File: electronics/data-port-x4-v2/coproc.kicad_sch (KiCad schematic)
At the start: 42 parts, among them U11 RP2354B, Y2 ABM8-272-T3

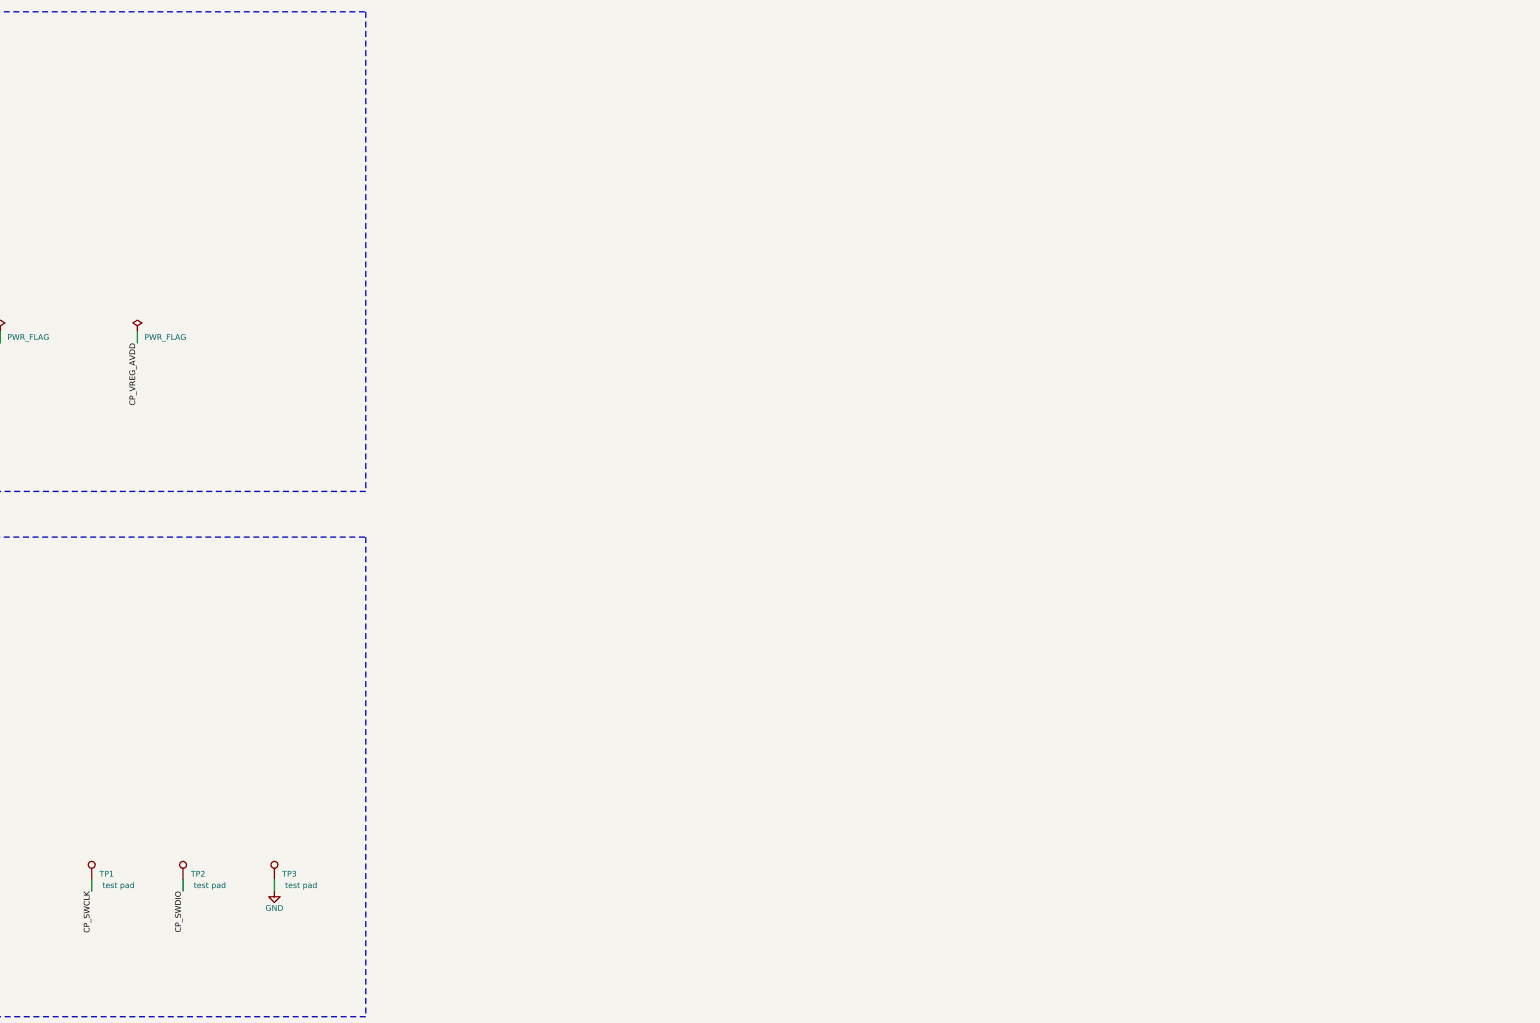
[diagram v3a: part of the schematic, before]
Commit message: DATA x4 v2: 32 labelled bring-up test points on the rear face
Eve's DFT rule on the DATA x4 v2.  Bare pads on B.Cu, mask open, no
paste, out of the BOM and the CPL (no part, no fee).  Each is named on
B.SilkS.  Supplies and GND are 1.5 mm, signals 1.0 mm (main's
"testpad1").  One table in design.py (TPS) holds every position, and
each sheet places its own.

- Co-processor row along the top edge: BOOT, RUN, SWDIO, SWCLK, GND,
  +3V3_CP.  SWD moves here from the front face.  +1V1 sits under the
  chip, on its own rear track.
- Matrix, left column: DAT, CK, STB2, GND, -5V, +5V_MX, GND; STB1 and
  MX RST on their own rear tracks.
- Supplies by the LDO: +3V3, GND, the lead's +5V.
- Hub: HUB RST, GND, 1V8.  Below J1: INT, SDA, SCL (the board side of
  the lead's isolation) and GND.
- Each port's FAULT_N (TP101-TP401) on its own rear track, and a GND by
  each pair's expander.
- Left out: VREF, RESET_N and BOOT_N (on the headers), the lead's lines
  (on J1) and the USB pairs.
- The logic's pads are marked LOGIC ONLY: the base leaves those parts
  off, so they float there.

Every pad is more than 2 mm from the THT pads and from J1, and clear of
the cradle ends, the push band and the notches.  The closest are TP23,
2.0 mm from J1's courtyard, and TP27, 2.1 mm from J101.

Routing: the old routing is seeded as protected wiring, so Freerouting
only adds the new links.  Where it gave up, the pad sits on a rear track
of its own net, or a short drawn link joins it (RUN onto CP_RUN's track,
+3V3_CP through a via to FB2).  The import's tidy pass is applied.

Checks: ERC 0, DRC 0 errors, unconnected 0, parity 0.  The 4
silk_over_copper warnings are the same on main.  Flow-through ESD check
BAD 0.  The fab outputs, panel, renders and GLBs are regenerated; the
BOM and CPL are unchanged.  docs/electronics.md lists the points, and
the "Test pads" table gains the board.

Co-Authored-By: Claude Opus 5.5 <noreply@anthropic.com>
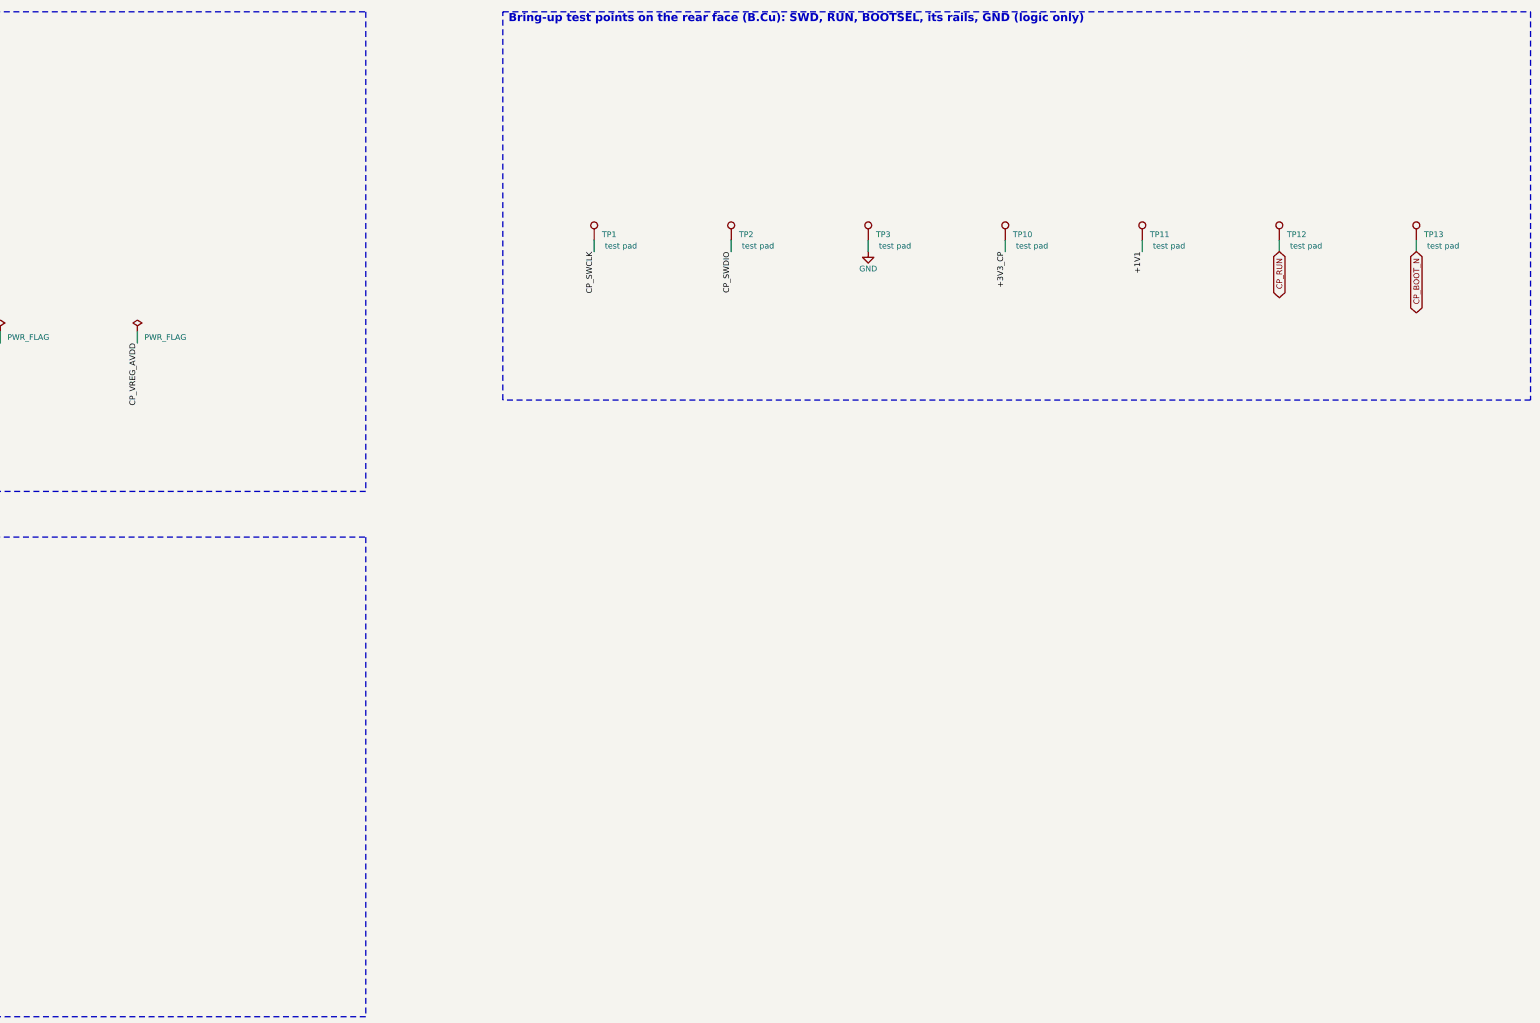
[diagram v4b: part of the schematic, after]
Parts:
- added TP10, TP11: test pad, TestPoint:TestPoint_Pad_D1.5mm, symbol Connector:TestPoint
- added TP12, TP13: test pad, TestPoint:TestPoint_Pad_D1.0mm, symbol Connector:TestPoint
- TP1, TP2: footprint TestPoint:TestPoint_Pad_D1.5mm -> TestPoint:TestPoint_Pad_D1.0mm
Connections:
- net +1V1: now also TP11.1
- net +3V3_CP: now also TP10.1
- net CP_BOOT_N: now also TP13.1
- net CP_RUN: now also TP12.1
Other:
- note added: "Bring-up test points on the rear face (B.Cu): SWD, RUN, BOOTSEL, its rails, GND (logic only)"
- moved on the sheet: TP1, TP2, TP3

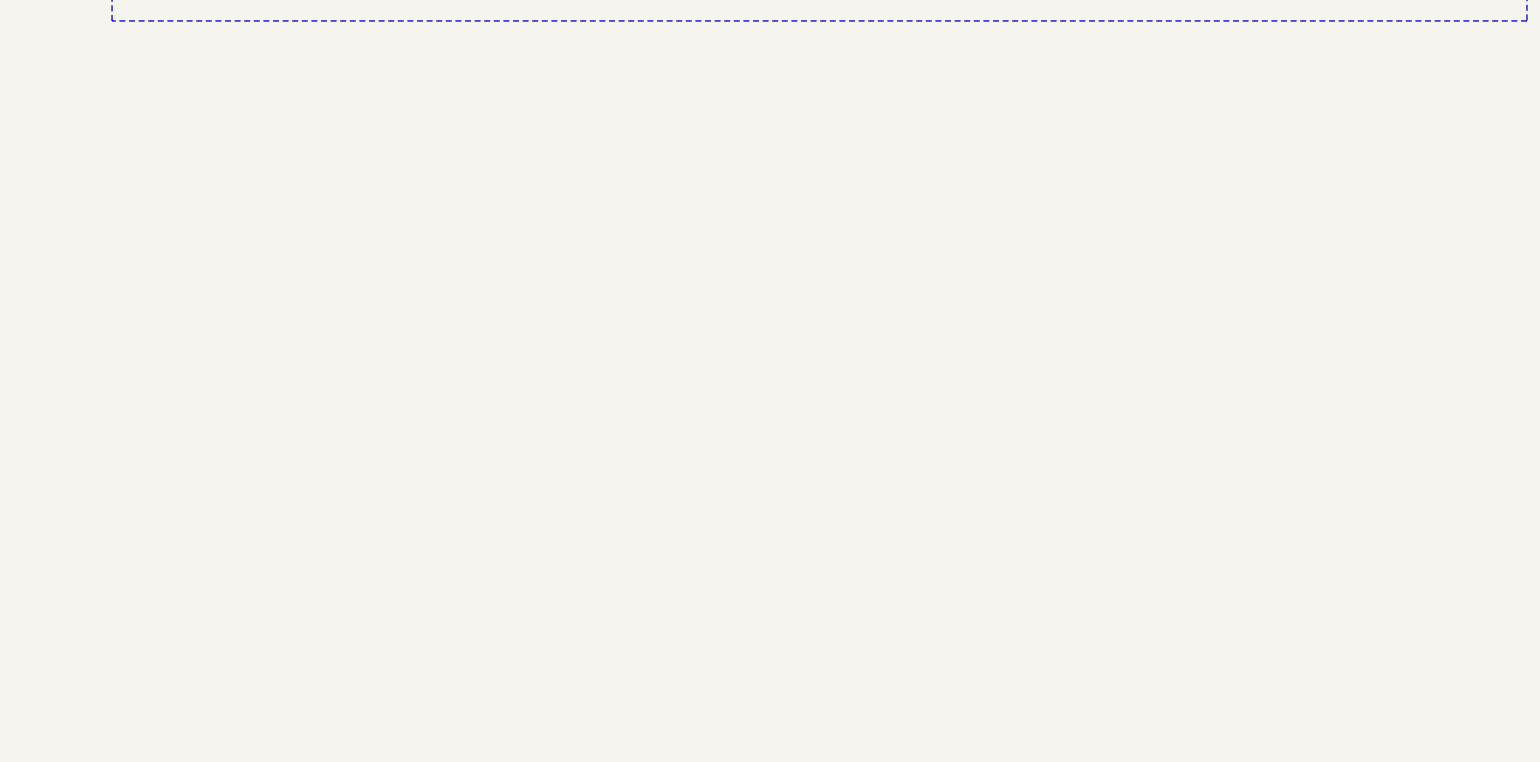
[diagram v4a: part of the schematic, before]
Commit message: DATA x4 v2: a 1x5 SWD header for the co-processor (logic only)
The user wants a classic header to reprogram the RP2354B, as Eve
suggested, and the rear test points stay as they are.

- J2 is a 1x5 2.54 mm through-hole header, hanxia HX PZ2.54-1x5P ZZ
  (C32713271), soldered by hand.
  - Pins: 1 SWCLK, 2 GND, 3 SWDIO, 4 RUN, 5 3V3.  Pins 1-3 follow the
    Pico 2's debug order, so the Raspberry Pi Debug Probe's 3-pin lead
    plugs straight on.  RUN and 3V3 serve a J-Link or an ST-Link on
    Dupont wires.
  - 3V3 is the probe's VTref: the board's +3V3, on the In2 plane there.
    +3V3_CP is the same rail through FB2, and its island ends at x 53.
- Placement: the front face's top edge, right of the co-processor
  (x 59.2-69.4, z about 68.5).
  - Both faces are free there.  The nearest rear test point is 6 mm
    away, and every test pad is more than 2 mm from J2's pads.
  - A probe reaches it from above with the board in its cradle.  The
    comb and the strip are at the bottom edge.  A box4 cover lifts off
    first: the pins stop 1 mm short of its front wall.
- Silkscreen: the pin names spelled out on the front face, alternately
  over and under the pins from pin 1 (west).
- No via within 1.6 mm of J2's pins (a vias-only keepout).  A GND
  stitching via had landed 0.4 mm from pin 1's pad, and a solder bridge
  there would ground SWCLK.
- Routing: the old routing was seeded as protected wiring.  Freerouting
  left SWCLK and SWDIO open and ran RUN in jogs, so all three are drawn
  in design.py: three parallel lines on the rear face along the top
  edge, up through a via onto each net's existing copper.
  - CP_RUN's drawn line moves from y 1.75 to y 1.85, TP12's stub with
    it.
  - The SWD lines pass under the crystal, which moved the auto GND
    fan-outs of D1, Y2 and C43 onto other routes.  Those three are drawn
    now: Y2's and C43's where they were, D1's straight under its pad.
- Checks:
  - ERC 0.  DRC empty on the board and the panel, unconnected 0,
    pari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
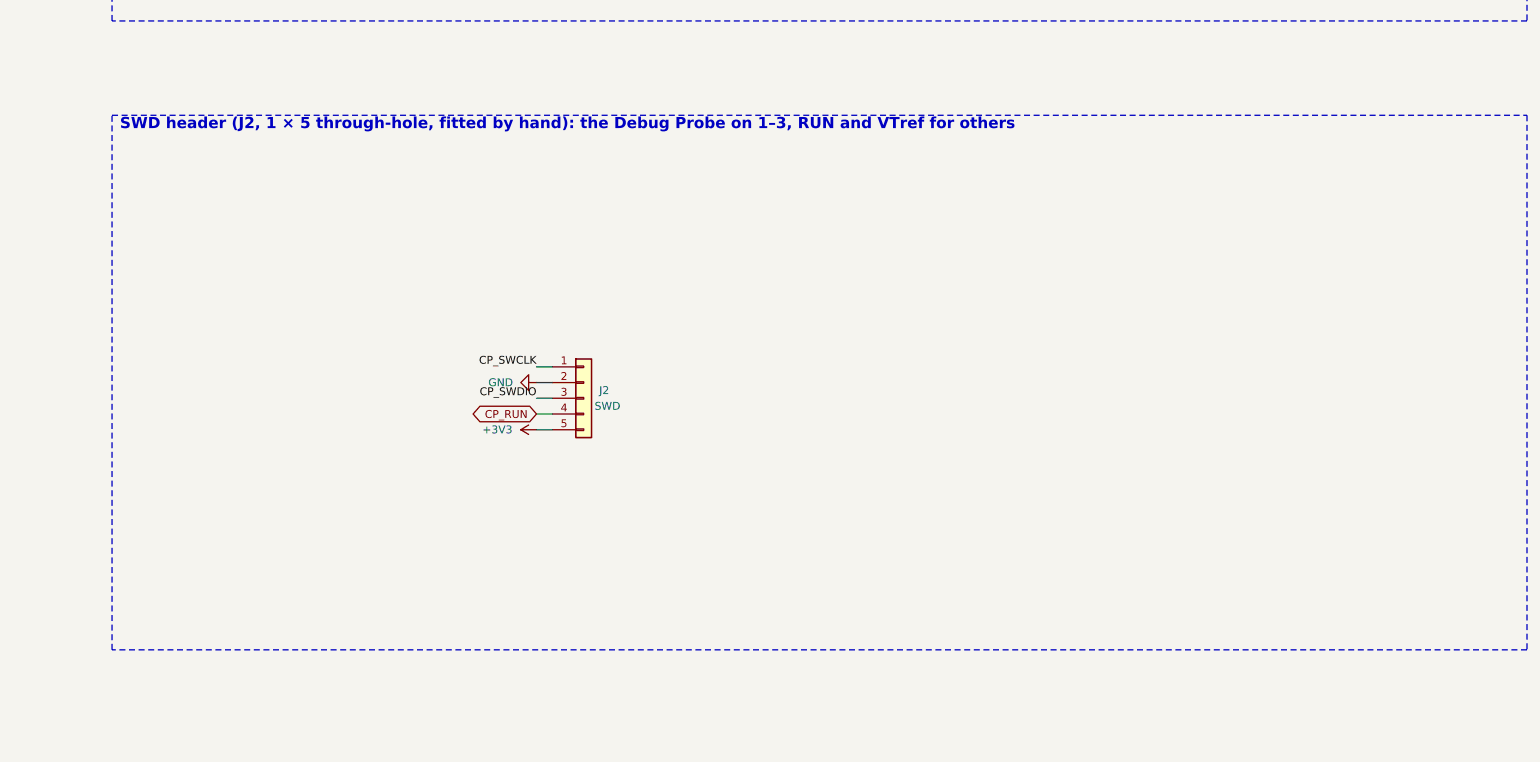
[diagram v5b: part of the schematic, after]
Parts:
- added J2: SWD, Connector_PinHeader_2.54mm:PinHeader_1x05_P2.54mm_Vertical, symbol Connector_Generic:Conn_01x05
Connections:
- net +3V3: now also J2.5 (Pin_5)
- net CP_RUN: now also J2.4 (Pin_4)
- net CP_SWCLK: now also J2.1 (Pin_1)
- net CP_SWDIO: now also J2.3 (Pin_3)
- net GND: now also J2.2 (Pin_2)
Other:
- note added: "SWD header (J2, 1 × 5 through-hole, fitted by hand): the Debug Probe on 1–3, RUN and VTref for others"
